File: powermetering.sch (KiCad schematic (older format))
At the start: 156 parts, among them J1 Conn_01x04, J2 Conn_01x02, J3 Conn_01x02, J4 Conn_01x02, J5 Conn_01x02, U2 ADE9000, U5 ALTAIR04-900, U6 AP1117-50, U7 Si8641ED-B-IS2, U8 NXE2S0505MC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

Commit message: finish routing of bottom board
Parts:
- added C75: 470µ, Capacitor_SMD:CP_Elec_8x10.5, symbol stmbl:CP
- added C76: 100n, stmbl:C_0805, symbol stmbl:C
- added J7, J8, J9: CONN_01X02, stmbl:Pin_Header_Straight_1x02, symbol stmbl:CONN_01X02
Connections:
- net labels added: MISO, MOSI, SCLK, SS
- wire segments 489 -> 532

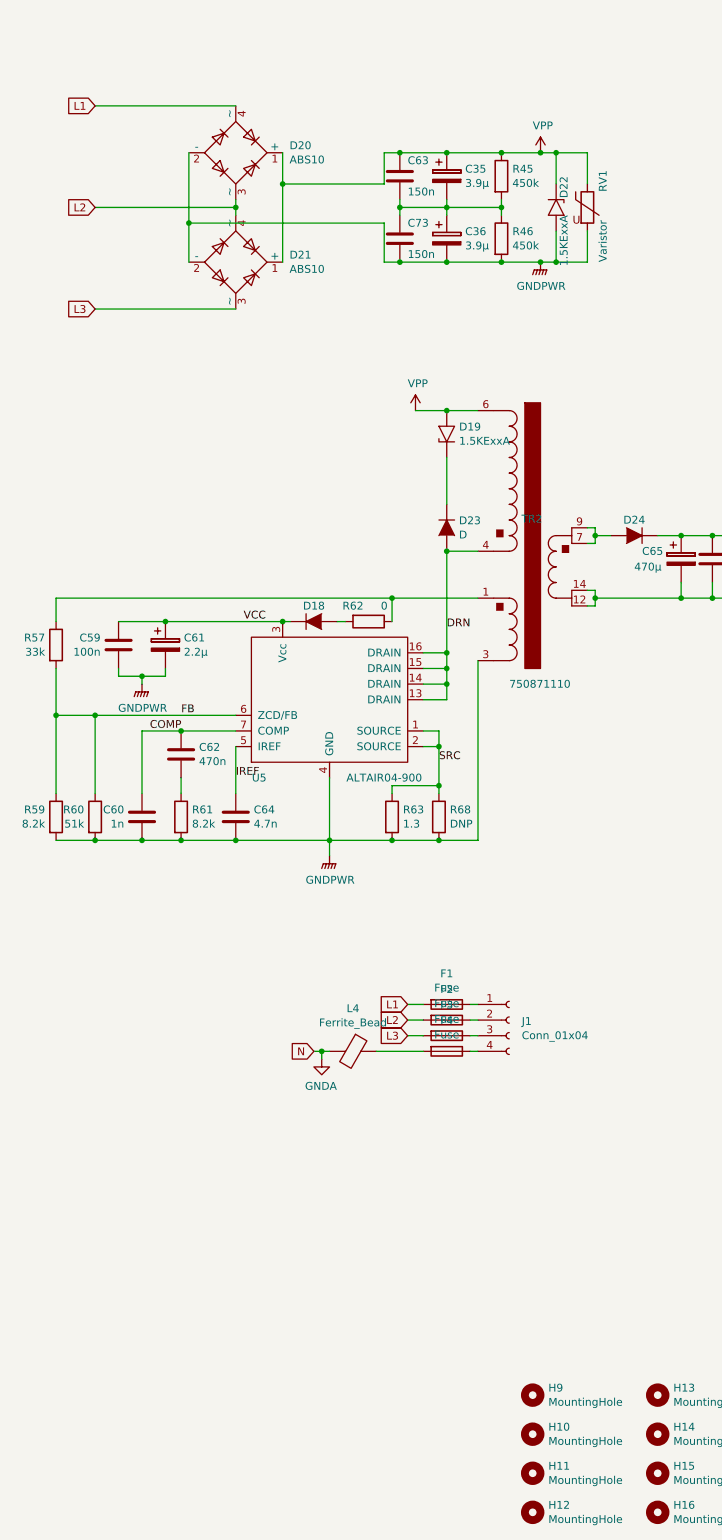
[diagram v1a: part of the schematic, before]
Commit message: finalize proto board and add second board outline
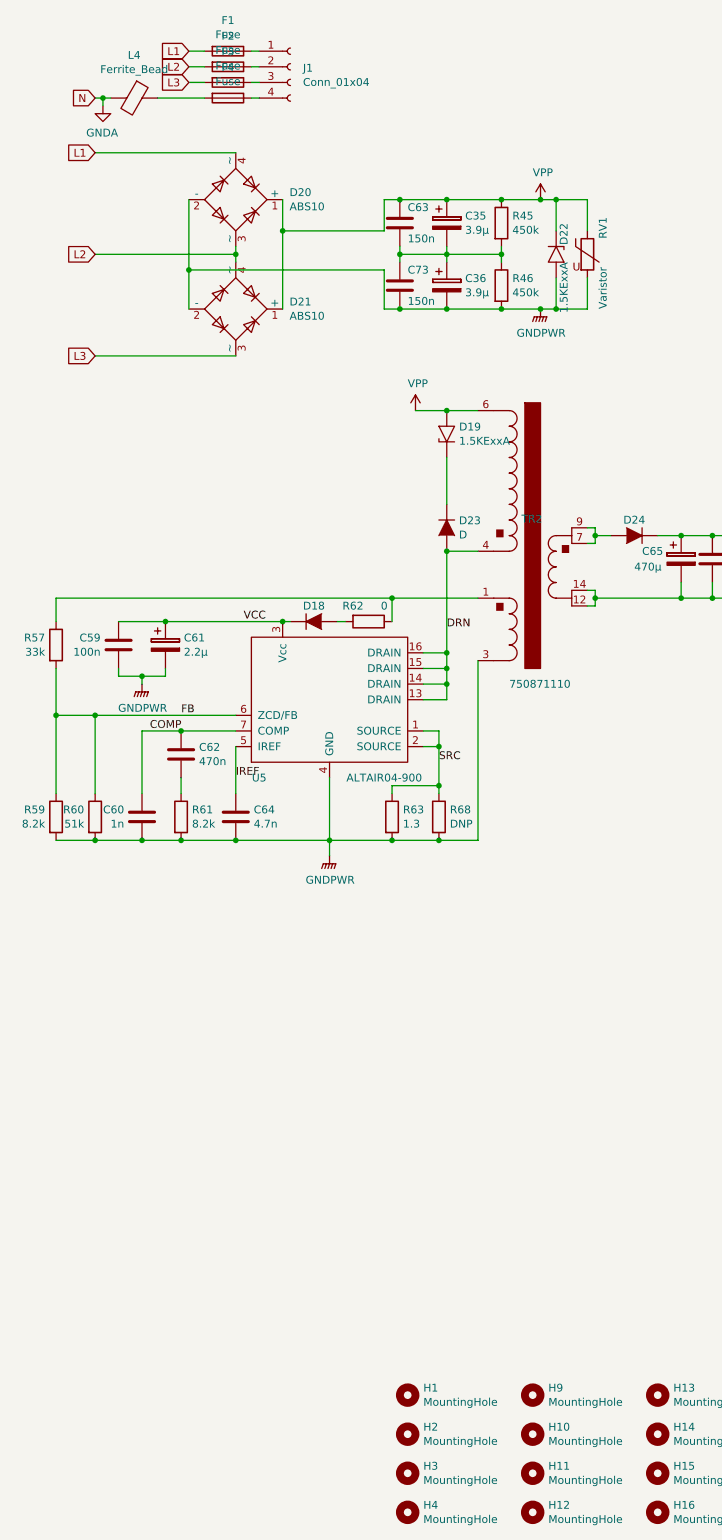
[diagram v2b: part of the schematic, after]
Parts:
- added H1, H2, H3, H4: MountingHole, MountingHole:MountingHole_3.2mm_M3, symbol Mechanical:MountingHole
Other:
- moved on the sheet: C35, C36, C63, C73, D20, D21, D22, F1, F2, F3, F4, J1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

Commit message: move fuses, add power header
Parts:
- added BT1: Battery_Cell, Battery:BatteryHolder_Keystone_1042_1x18650, symbol Device:Battery_Cell
- added C55, C81: 1µ, stmbl:C_0805, symbol stmbl:C
- added C80, C83, C84: 100n, stmbl:C_0805, symbol stmbl:C
- added C82: 470µ, Capacitor_SMD:CP_Elec_8x10.5, symbol stmbl:CP
- added J11, J12, J13, J14, J15: CONN_01X02, stmbl:Pin_Header_Straight_1x02, symbol stmbl:CONN_01X02
- added R55: 330, stmbl:R_0805, symbol stmbl:R
- added R69: 2.7k, stmbl:R_0805, symbol stmbl:R
- added U10: AP1117-50, Package_TO_SOT_SMD:SOT-223-3_TabPin2, symbol Regulator_Linear:AP1117-50
- added U11: AP9101CK, Package_TO_SOT_SMD:SOT-23-5, symbol Battery_Management:AP9101CK
- added U12, U13: NFET, stmbl:SOT-23, symbol stmbl:NFET
- added U9: MCP73811T-420I-OT, Package_TO_SOT_SMD:SOT-23-5, symbol Battery_Management:MCP73811T-420I-OT
- F1, F2, F3, F4: footprint Fuse:Fuseholder_Cylinder-6.3x32mm_Schurter_0031-8002_Horizontal_Open -> Fuse:Fuse_SunFuse-6HP
- RV1: footprint (none) -> Varistor:RV_Disc_D12mm_W3.9mm_P7.5mm
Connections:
- net labels added: +BATT
- wire segments 532 -> 590
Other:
- note added: "Li cell ground != GNDA"
- moved on the sheet: H1, H10, H11, H12, H13, H14, H15, H16, H2, H3, H4, H9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

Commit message: V2 hardware
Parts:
- removed D10, D11, D12, D13, D14, D15, D16, D17, D2, D3, D4, D5, D6, D7, D8, D9: D, stmbl:SMA_Standard, symbol stmbl:D
- removed J11: CONN_01X02, stmbl:Pin_Header_Straight_1x02, symbol stmbl:CONN_01X02
- removed U7: Si8641ED-B-IS2, Package_SO:SOIC-16W_7.5x10.3mm_P1.27mm, symbol Isolator:Si8641ED-B-IS2
- added D2, D3, D4, D5, D6, D7, D8, D9: D_Schottky_x2_Serial_AKC, Package_TO_SOT_SMD:SOT-23, symbol Device:D_Schottky_x2_Serial_AKC
- added D25, D26: D, stmbl:SMA_Standard, symbol stmbl:D
- added RV2, RV3, RV4: Varistor, Varistor:RV_Disc_D12mm_W3.9mm_P7.5mm, symbol Device:Varistor
- added U7: Si8641EB-B-IU, Package_SO:QSOP-16_3.9x4.9mm_P0.635mm, symbol Isolator:Si8641EB-B-IU
- BT1: footprint Battery:BatteryHolder_Keystone_1042_1x18650 -> powermetering:18650_keystone_54
- D19, D22: footprint stmbl:SMA_Standard -> Diode_SMD:D_SMC
- R34, R35, R36, R37, R38, R39, R40, R41: footprint Resistor_SMD:R_2010_5025Metric -> Resistor_SMD:R_0612_1632Metric
- Y1: footprint stmbl-kicad-lib:Crystal_SMD_0603_4Pads -> Crystal:Crystal_SMD_3225-4Pin_3.2x2.5mm; symbol stmbl:Crystal -> Device:Crystal_GND24
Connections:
- net labels added: GNDS
- wire segments 590 -> 568

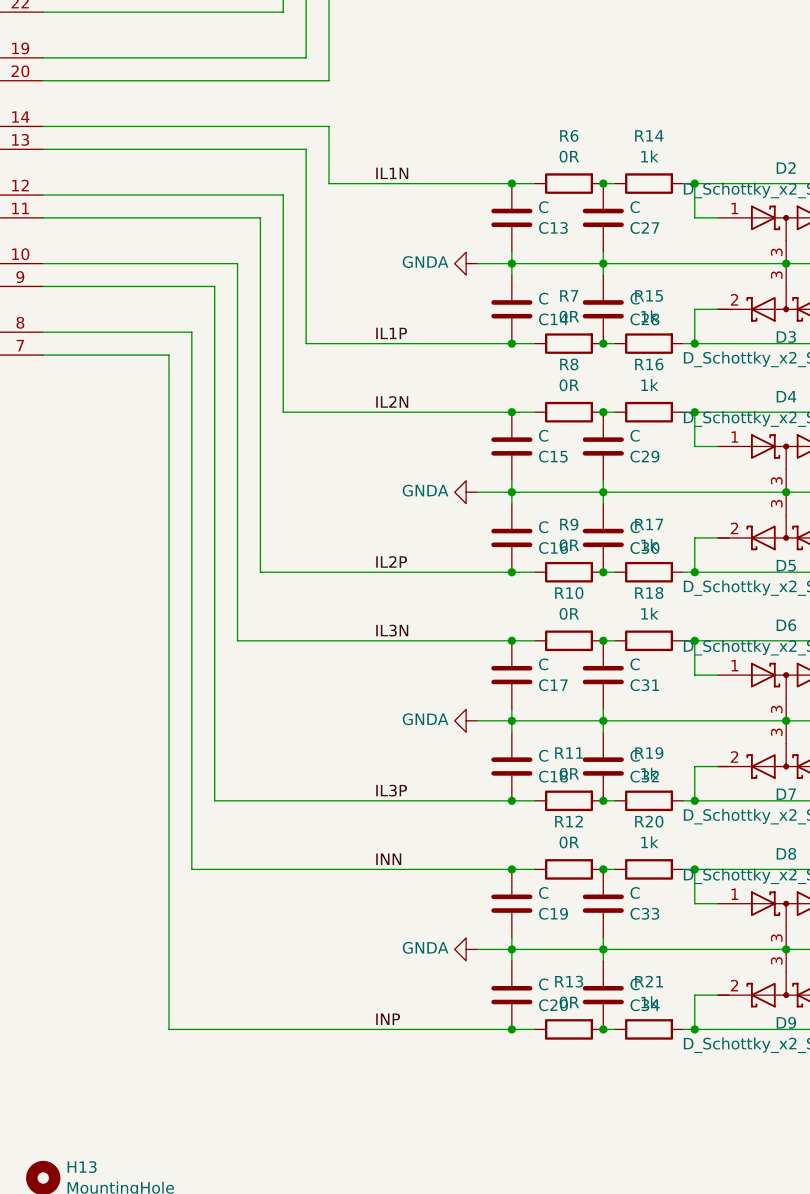
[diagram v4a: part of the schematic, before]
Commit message: swap phase order on current input
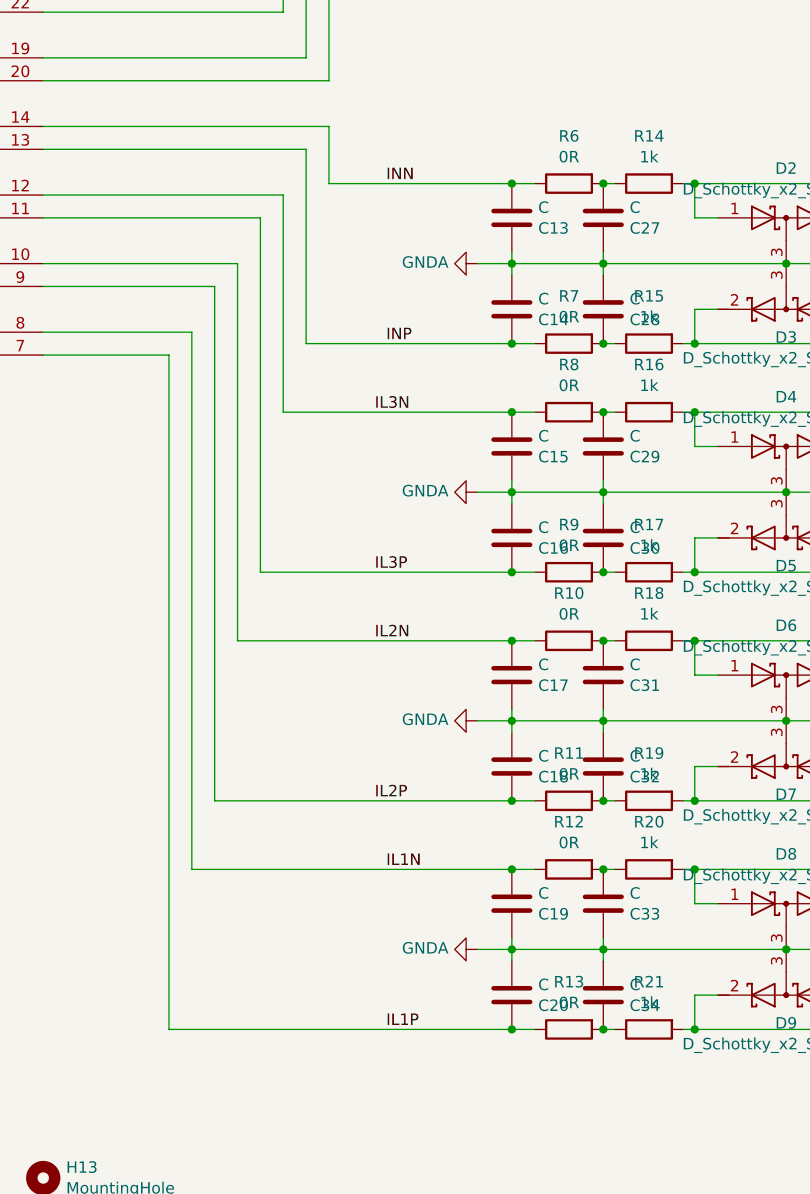
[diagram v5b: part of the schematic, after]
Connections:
- net IL1N: now also C19.1, R12.1, U2.8 (IAN); no longer C13.1, R6.1, U2.14 (INN)
- net IL1P: now also C20.2, R13.1, U2.7 (IAP); no longer C14.2, R7.1, U2.13 (INP)
- net IL2N: now also C17.1, R10.1, U2.10 (IBN); no longer C15.1, R8.1, U2.12 (ICN)
- net IL2P: now also C18.2, R11.1, U2.9 (IBP); no longer C16.2, R9.1, U2.11 (ICP)
- net IL3N: now also C15.1, R8.1, U2.12 (ICN); no longer C17.1, R10.1, U2.10 (IBN)
- net IL3P: now also C16.2, R9.1, U2.11 (ICP); no longer C18.2, R11.1, U2.9 (IBP)
- net INN: now also C13.1, R6.1, U2.14 (INN); no longer C19.1, R12.1, U2.8 (IAN)
- net INP: now also C14.2, R7.1, U2.13 (INP); no longer C20.2, R13.1, U2.7 (IAP)
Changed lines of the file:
@@
 Text Label 12550 4350 0    50   ~ 0
 UL1N
-Text Label 11950 5850 0    50   ~ 0
+Text Label 12000 8850 0    50   ~ 0
 IL1N
+Text Label 11950 7850 0    50   ~ 0
+IL2N
 Text Label 11950 6850 0    50   ~ 0
-IL2N
-Text Label 11950 7850 0    50   ~ 0
 IL3N
-Text Label 11950 6550 0    50   ~ 0
+Text Label 12000 9550 0    50   ~ 0
 IL1P
+Text Label 11950 8550 0    50   ~ 0
+IL2P
 Text Label 11950 7550 0    50   ~ 0
-IL2P
-Text Label 11950 8550 0    50   ~ 0
 IL3P
-Text Label 11950 9550 0    50   ~ 0
+Text Label 12000 6550 0    50   ~ 0
 INP
-Text Label 11950 8850 0    50   ~ 0
+Text Label 12000 5850 0    50   ~ 0
 INN
 Text Label 9750 4200 1    50   ~ 0

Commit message: add EMI capacitor
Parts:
- added C79: C, Capacitor_SMD:C_1806_4516Metric, symbol Device:C
- J1: footprint TerminalBlock_Phoenix:TerminalBlock_Phoenix_PT-1,5-4-5.0-H_1x04_P5.00mm_Horizontal -> TerminalBlock_Phoenix:TerminalBlock_Phoenix_PT-1,5-5-5.0-H_1x05_P5.00mm_Horizontal; symbol Connector:Conn_01x04_Female -> Connector:Conn_01x05_Female
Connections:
- net GND: now also C79.1
- net VCC: no longer U5.3 (Vcc)
- new net Earth_Protective: C79.2, J1.5 (Pin_5)
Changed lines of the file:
@@
-EESchema Schematic File Version 4
+EESchema Schematic File Version 5
 LIBS:powermetering-cache
 EELAYER 29 0
@@
 $EndComp
 $Comp
-L Connector:Conn_01x04_Female J1
+L Connector:Conn_01x05_Female J1
 U 1 1 5C2E6576
-P 2300 850
-F 0 "J1" H 2380 842 50  0000 L CNN
-F 1 "Conn_01x04" H 2380 751 50  0000 L CNN
-F 2 "TerminalBlock_Phoenix:TerminalBlock_Phoenix_PT-1,5-4-5.0-H_1x04_P5.00mm_Horizontal" H 2300 850 50  0001 C CNN
-F 3 "~" H 2300 850 50  0001 C CNN
-	1    2300 850
+P 2300 950
+F 0 "J1" H 2380 942 50  0000 L CNN
+F 1 "Conn_01x04" H 2380 851 50  0000 L CNN
+F 2 "TerminalBlock_Phoenix:TerminalBlock_Phoenix_PT-1,5-5-5.0-H_1x05_P5.00mm_Horizontal" H 2300 950 50  0001 C CNN
+F 3 "~" H 2300 950 50  0001 C CNN
+	1    2300 950
 	1    0    0    -1
 $EndComp
@@
 	3300 3050 3500 3050
 Connection ~ 3300 3950
-Connection ~ 2250 4400
-Wire Wire Line
-	2250 4400 2300 4400
 Connection ~ 1600 5100
 Wire Wire Line
@@
 Connection ~ 1500 4400
 Wire Wire Line
-	1500 4400 2250 4400
-Wire Wire Line
 	10800 3850 10800 3900
 Connection ~ 8300 6250
@@
 Wire Wire Line
 	1600 7000 1800 7000
+$Comp
+L stmbl:Earth_Protective #PWR0195
+U 1 1 5D1CC365
+P 1950 1250
+F 0 "#PWR0195" H 2200 1000 50  0001 C CNN
+F 1 "Earth_Protective" H 2400 1100 50  0001 C CNN
+F 2 "" H 1950 1150 50  0001 C CNN
+F 3 "" H 1950 1150 50  0001 C CNN
+	1    1950 1250
+	0    1    1    0
+$EndComp
+Wire Wire Line
+	2100 1150 2100 1250
+Wire Wire Line
+	2100 1250 1950 1250
+$Comp
+L stmbl:Earth_Protective #PWR0196
+U 1 1 5D1CE6B6
+P 7550 4600
+F 0 "#PWR0196" H 7800 4350 50  0001 C CNN
+F 1 "Earth_Protective" H 8000 4450 50  0001 C CNN
+F 2 "" H 7550 4500 50  0001 C CNN
+F 3 "" H 7550 4500 50  0001 C CNN
+	1    7550 4600
+	1    0    0    -1
+$EndComp
+Wire Wire Line
+	1500 4400 2300 4400
+$Comp
+L Device:C C79
+U 1 1 5D1D12E2
+P 7200 4600
+F 0 "C79" V 7452 4600 50  0000 C CNN
+F 1 "C" V 7361 4600 50  0000 C CNN
+F 2 "Capacitor_SMD:C_1806_4516Metric" H 7238 4450 50  0001 C CNN
+F 3 "~" H 7200 4600 50  0001 C CNN
+	1    7200 4600
+	0    -1   -1   0
+$EndComp
+$Comp
+L stmbl:GND #PWR0197
+U 1 1 5D1D1BDE
+P 6850 4600
+F 0 "#PWR0197" H 6850 4350 50  0001 C CNN
+F 1 "GND" H 6855 4427 50  0000 C CNN
+F 2 "" H 6850 4600 50  0001 C CNN
+F 3 "" H 6850 4600 50  0001 C CNN
+	1    6850 4600
+	1    0    0    -1
+$EndComp
+Wire Wire Line
+	6850 4600 7050 4600
+Wire Wire Line
+	7350 4600 7550 4600
 $EndSCHEMATC

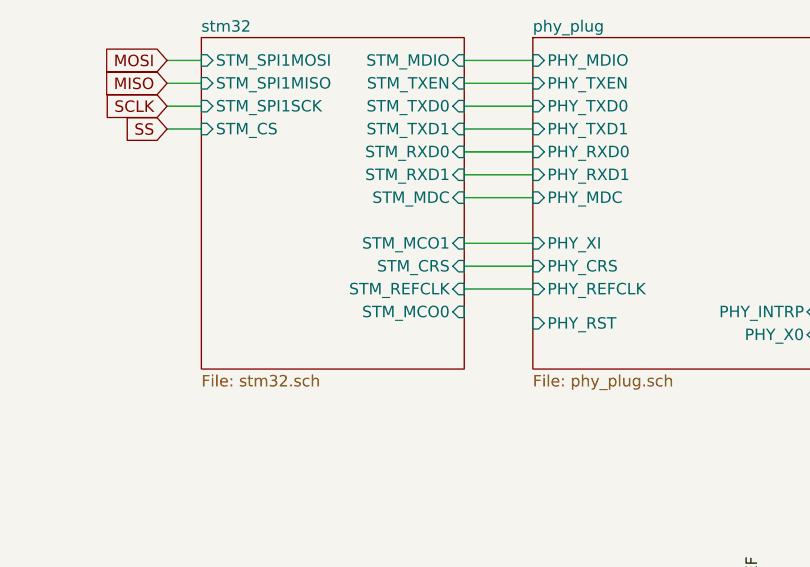
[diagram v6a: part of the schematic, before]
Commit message: add sd card holder
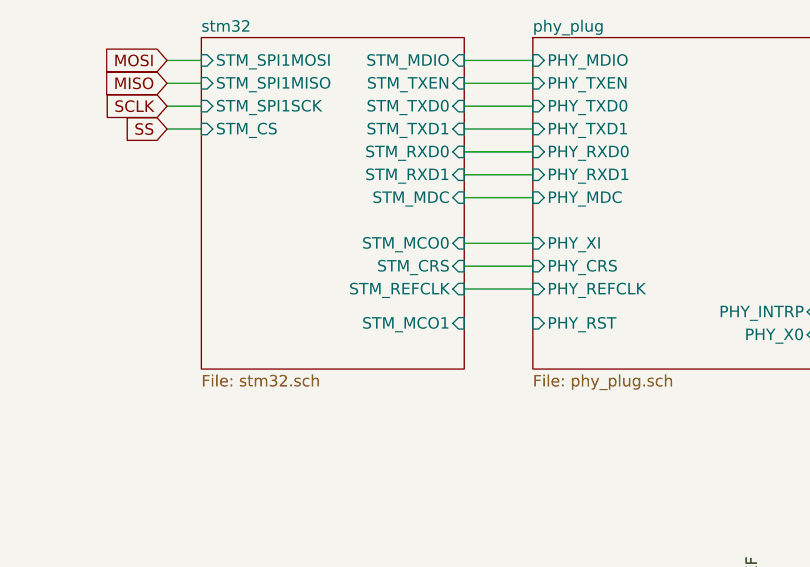
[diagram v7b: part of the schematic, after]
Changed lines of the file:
@@
 F7 "STM_TXD0" I R 8250 1200 50
 F8 "STM_MDC" I R 8250 1600 50
-F9 "STM_MCO1" I R 8250 1800 50
+F9 "STM_MCO1" I R 8250 2150 50
 F10 "STM_CRS" I R 8250 1900 50
 F11 "STM_SPI1MOSI" I L 7100 1000 50
@@
 F14 "STM_CS" I L 7100 1300 50
 F15 "STM_REFCLK" I R 8250 2000 50
-F16 "STM_MCO0" I R 8250 2100 50
+F16 "STM_MCO0" I R 8250 1800 50
 $EndSheet
 $Comp

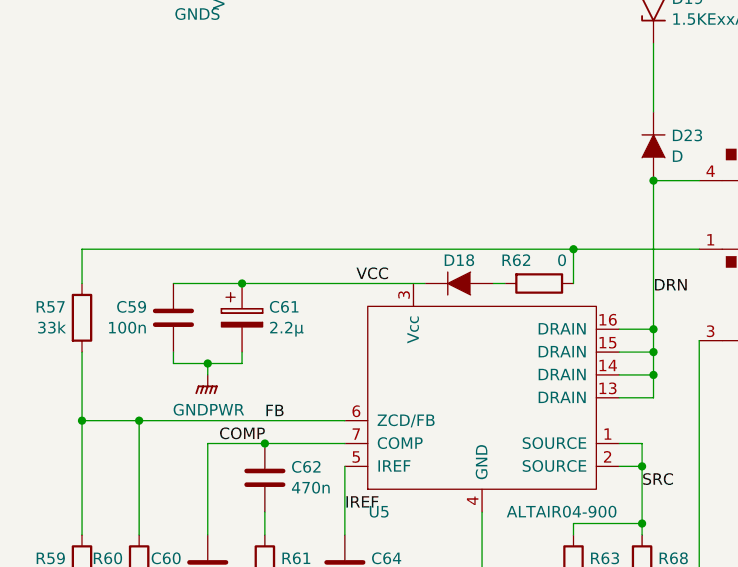
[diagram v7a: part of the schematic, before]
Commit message: add bodge pads and move stuff around
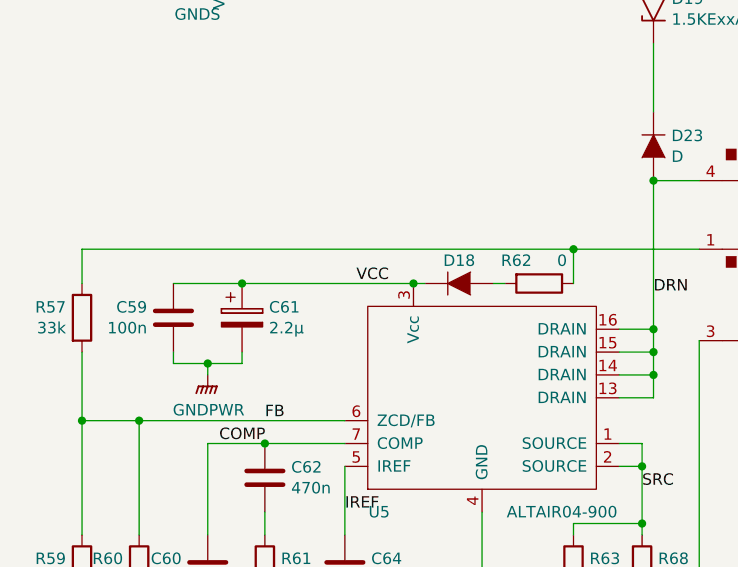
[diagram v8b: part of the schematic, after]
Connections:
- net VCC: now also U5.3 (Vcc)
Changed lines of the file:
@@
 $EndComp
 Wire Wire Line
-	1500 4400 2300 4400
+	1500 4400 2250 4400
 $Comp
 L Device:C C79
@@
 Wire Wire Line
 	7350 4600 7550 4600
+Connection ~ 2250 4400
+Wire Wire Line
+	2250 4400 2300 4400
 $EndSCHEMATC
